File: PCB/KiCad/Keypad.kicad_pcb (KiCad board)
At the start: 2 copper layers, 79.4 x 116.2 mm, 17 parts, among them SW1 SW_SPDT, U1 TP4056, U2 MT3608, U3 WeMos_D1_mini

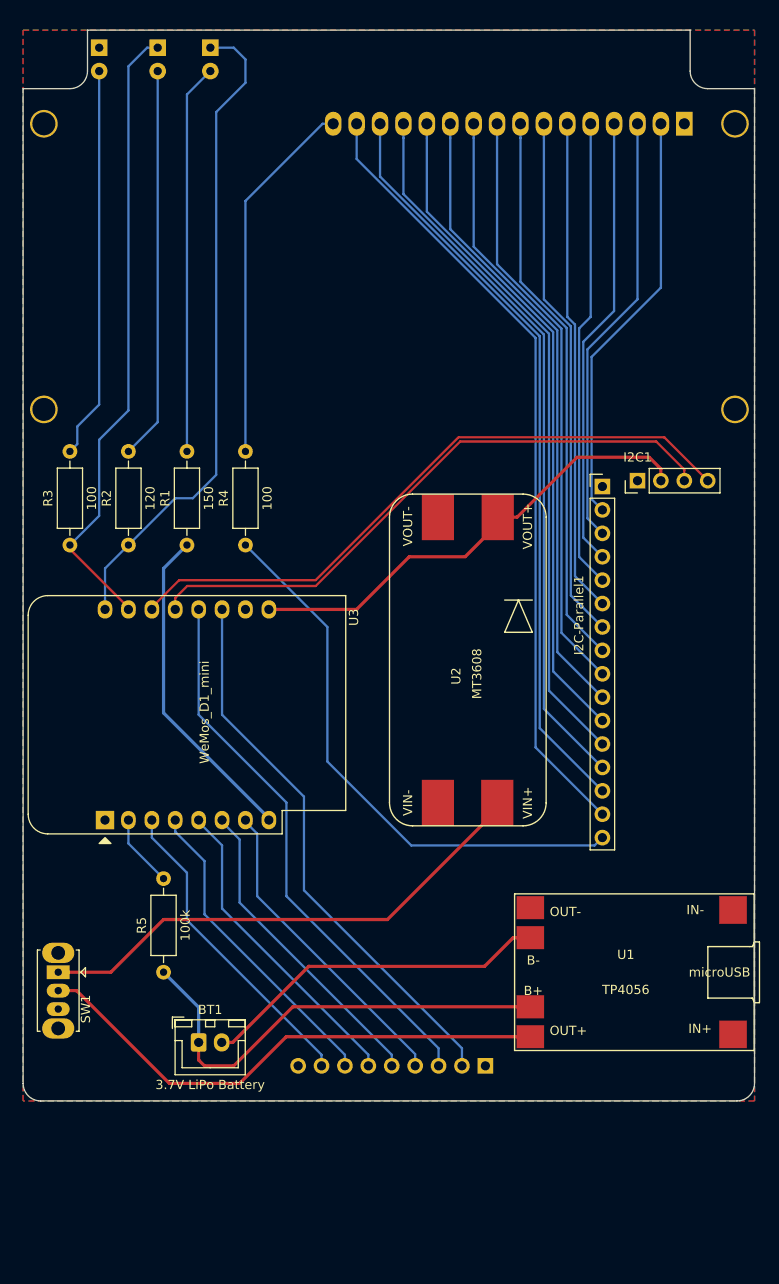
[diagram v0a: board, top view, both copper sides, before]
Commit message: Battery connections
Added direct SMD mounting points for a tabbed 18650 li-ion battery
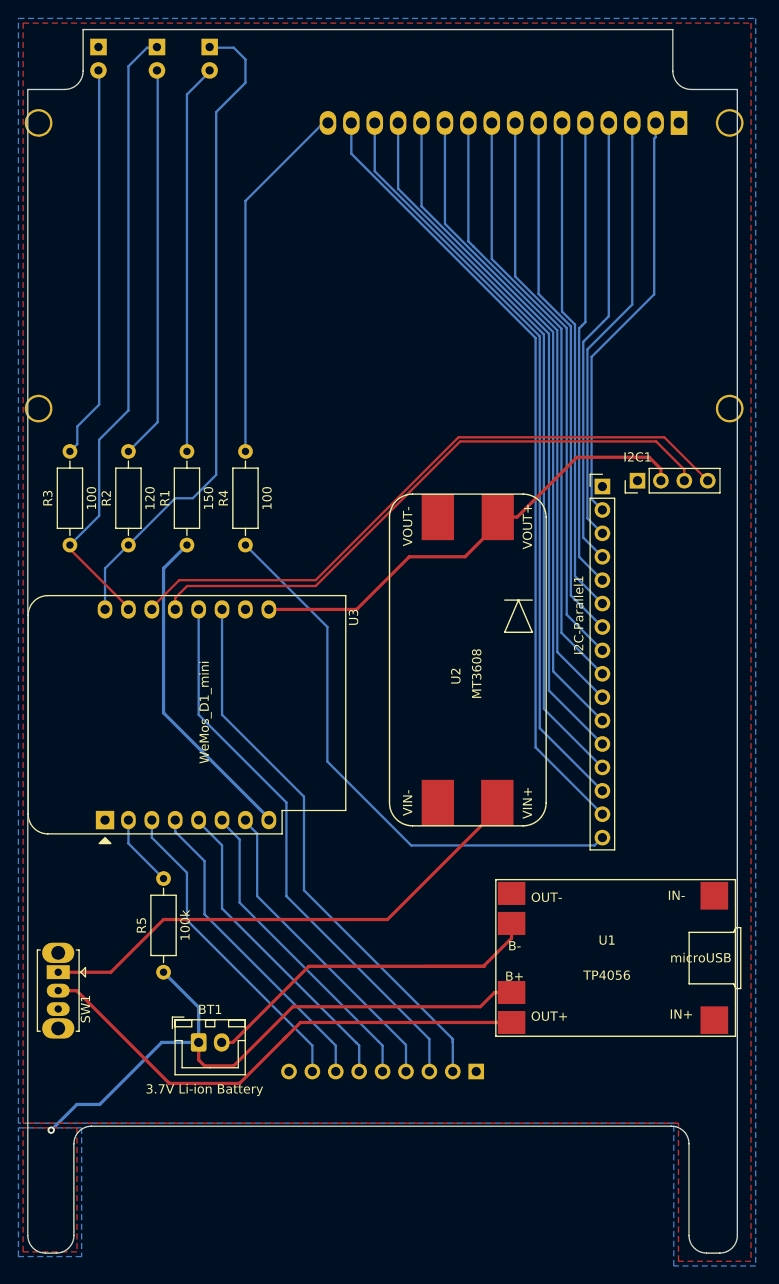
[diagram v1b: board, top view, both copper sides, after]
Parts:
- BT1: value 3.7V LiPo Battery -> 3.7V Li-ion Battery
- moved U1 2.55 mm to (174.5, 136.2)
- moved Keypad1 1.17 mm to (159.7, 148.6)
- moved DS1 0.58 mm to (181.7, 45.6)
- moved D1 0.11 mm to (130.7, 37.4)
- moved D2 0.11 mm to (125.0, 37.4)
- moved D3 0.11 mm to (118.7, 37.4)
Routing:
- net +BATT: track 50.0 -> 68.6 mm, vias 0 -> 1
- net -BATT: track 39.8 -> 44.2 mm
- net /V+1: track 57.5 -> 56.5 mm
- net /KP1: track 60.3 -> 61.0 mm
- added copper zone on B.Cu, net +BATT
- added copper zone on F.Cu, net +BATT
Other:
- board size 79.4 x 116.2 mm -> 77 x 132.8 mm
